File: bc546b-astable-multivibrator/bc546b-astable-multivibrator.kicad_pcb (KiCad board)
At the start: 2 copper layers, 40.4 x 57.3 mm, 19 parts

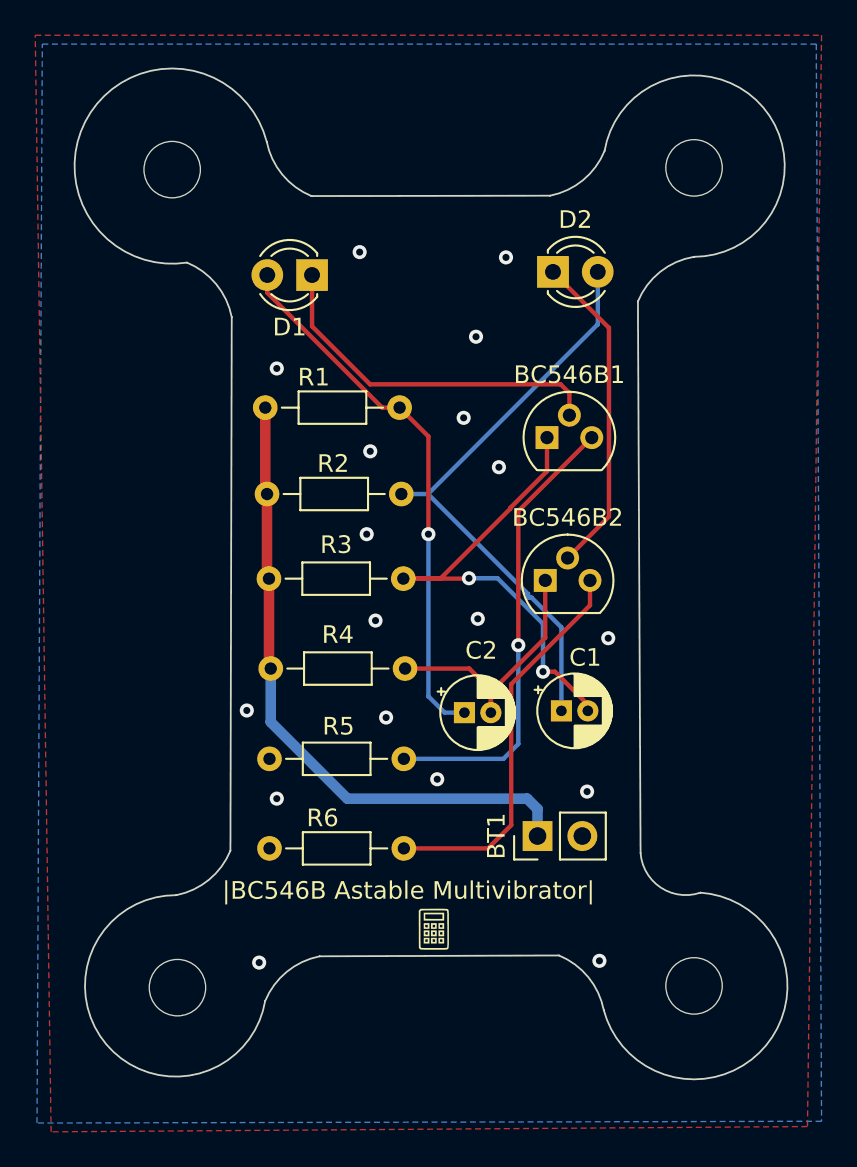
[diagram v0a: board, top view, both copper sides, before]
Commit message: project 6 / bc546b astable multivibrator / improved schematics, pcb after review
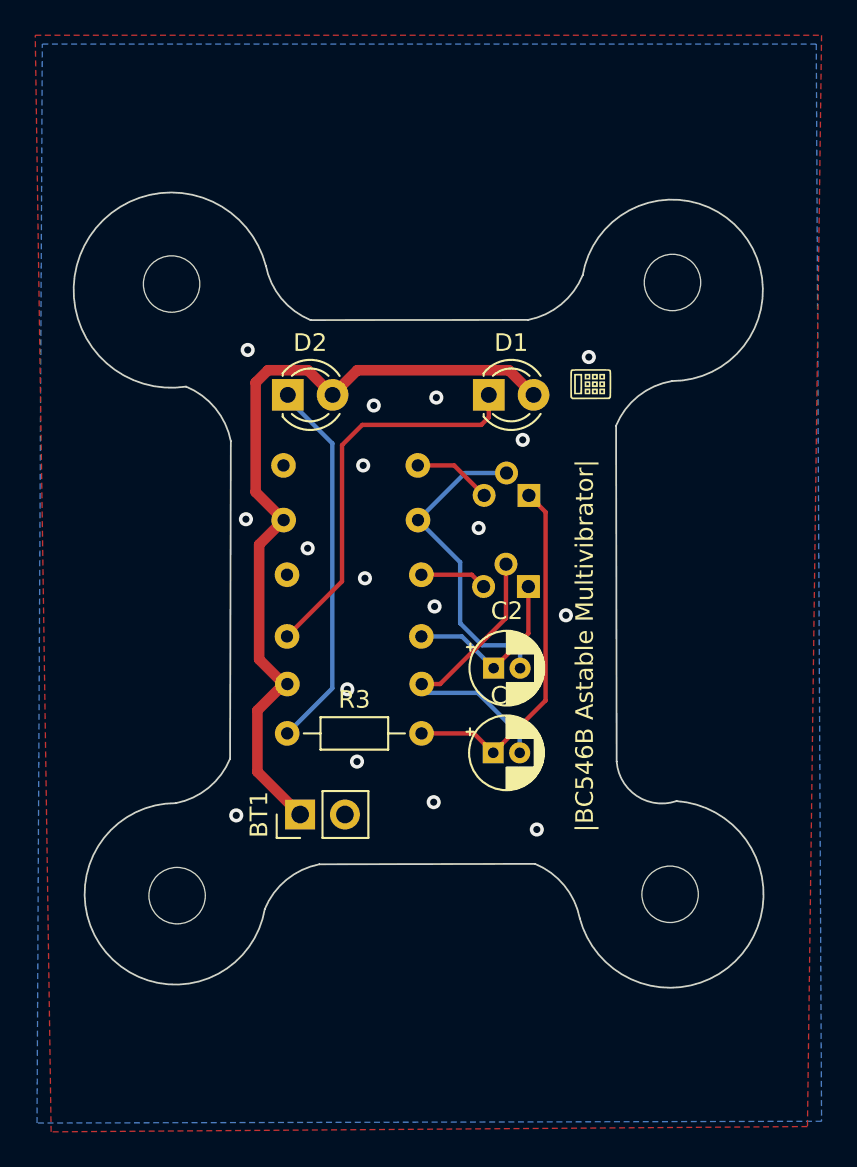
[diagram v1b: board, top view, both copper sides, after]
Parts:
- added G***: LOGO, Graphics:pcbLogo_30mmx30mm, B.Cu at (97.0, 69.5)
- BC546B1, BC546B2, R5, R6: moved to B.Cu
- C1, C2: value 100u -> 10u
- R1, R2: value 5k -> 100k; moved to B.Cu
- R3: value 1k -> 560
- R4: value 1k -> 560; moved to B.Cu
- moved G*** 32.2 mm to (106.6, 57.6), turned to 90 degrees
- moved R5 16.7 mm to (96.8, 62.2)
- moved D2 16.6 mm to (89.4, 58.2)
- moved R1 15.7 mm to (97.0, 74.6)
- moved R6 15.6 mm to (97.0, 68.4)
- moved BT1 13.5 mm to (90.1, 82.0)
- moved D1 12.1 mm to (100.8, 58.2), turned to 0 degrees
- moved R3 8.84 mm to (89.4, 77.4)
- moved R4 8.74 mm to (97.0, 71.9), turned to 180 degrees
- moved REF** 6.61 mm to (111.2, 51.8)
- moved REF** 6.49 mm to (82.8, 51.9)
- moved REF** 5.37 mm to (111.1, 86.5)
- moved REF** 5.22 mm to (83.1, 86.6)
- moved C1 4.54 mm to (101.1, 78.5)
- moved BC546B1 3.44 mm to (103.1, 63.9), turned to 180 degrees
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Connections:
- C1 pad 1: Net-(D2-A) -> Net-(BC546B1-C)
- C1 pad 2: Net-(BC546B1-C) -> /I1
- C2 pad 1: Net-(D1-A) -> Net-(BC546B2-C)
- C2 pad 2: Net-(BC546B2-C) -> /I2
- D1 pad 1: /I2 -> Net-(D1-K)
- D1 pad 2: Net-(D1-A) -> +9V
- D2 pad 1: /I1 -> Net-(D2-K)
- D2 pad 2: Net-(D2-A) -> +9V
- R1 pad 1: Net-(D1-A) -> /I1
- R2 pad 1: Net-(D2-A) -> /I2
- R3 pad 1: +9V -> Net-(D2-K)
- R4 pad 1: +9V -> Net-(BC546B2-C)
- R4 pad 2: Net-(BC546B2-C) -> Net-(D1-K)
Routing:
- net Net-(D2-A): track 33.7 -> 0.00 mm
- net Net-(D1-A): track 30.8 -> 0.00 mm, vias 1 -> 0
- net Net-(D1-K): track 0.00 -> 22.4 mm
- net Net-(BC546B1-E): track 26.0 -> 4.46 mm, vias 1 -> 0
- net Net-(D2-K): track 0.00 -> 21.3 mm
- net Net-(BC546B2-E): track 22.4 -> 3.81 mm
- net +9V: track 36.7 -> 45.7 mm
- net Net-(BC546B1-C): track 28.0 -> 20.7 mm, vias 2 -> 0
- net Net-(BC546B2-C): track 15.4 -> 10.3 mm
- net /I2: track 20.3 -> 17.9 mm
- net /I1: track 18.5 -> 17.4 mm
- net GND: vias 18 -> 17
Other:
- board size 40.4 x 57.3 mm -> 39.1 x 45.1 mm
